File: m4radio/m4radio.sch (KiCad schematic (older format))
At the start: 72 parts, among them IC1 MCP2562, IC2 STM32F405RxTx, J1 WEST TOP, J2 EAST TOP, P1 SWD_TC, Y1 26M

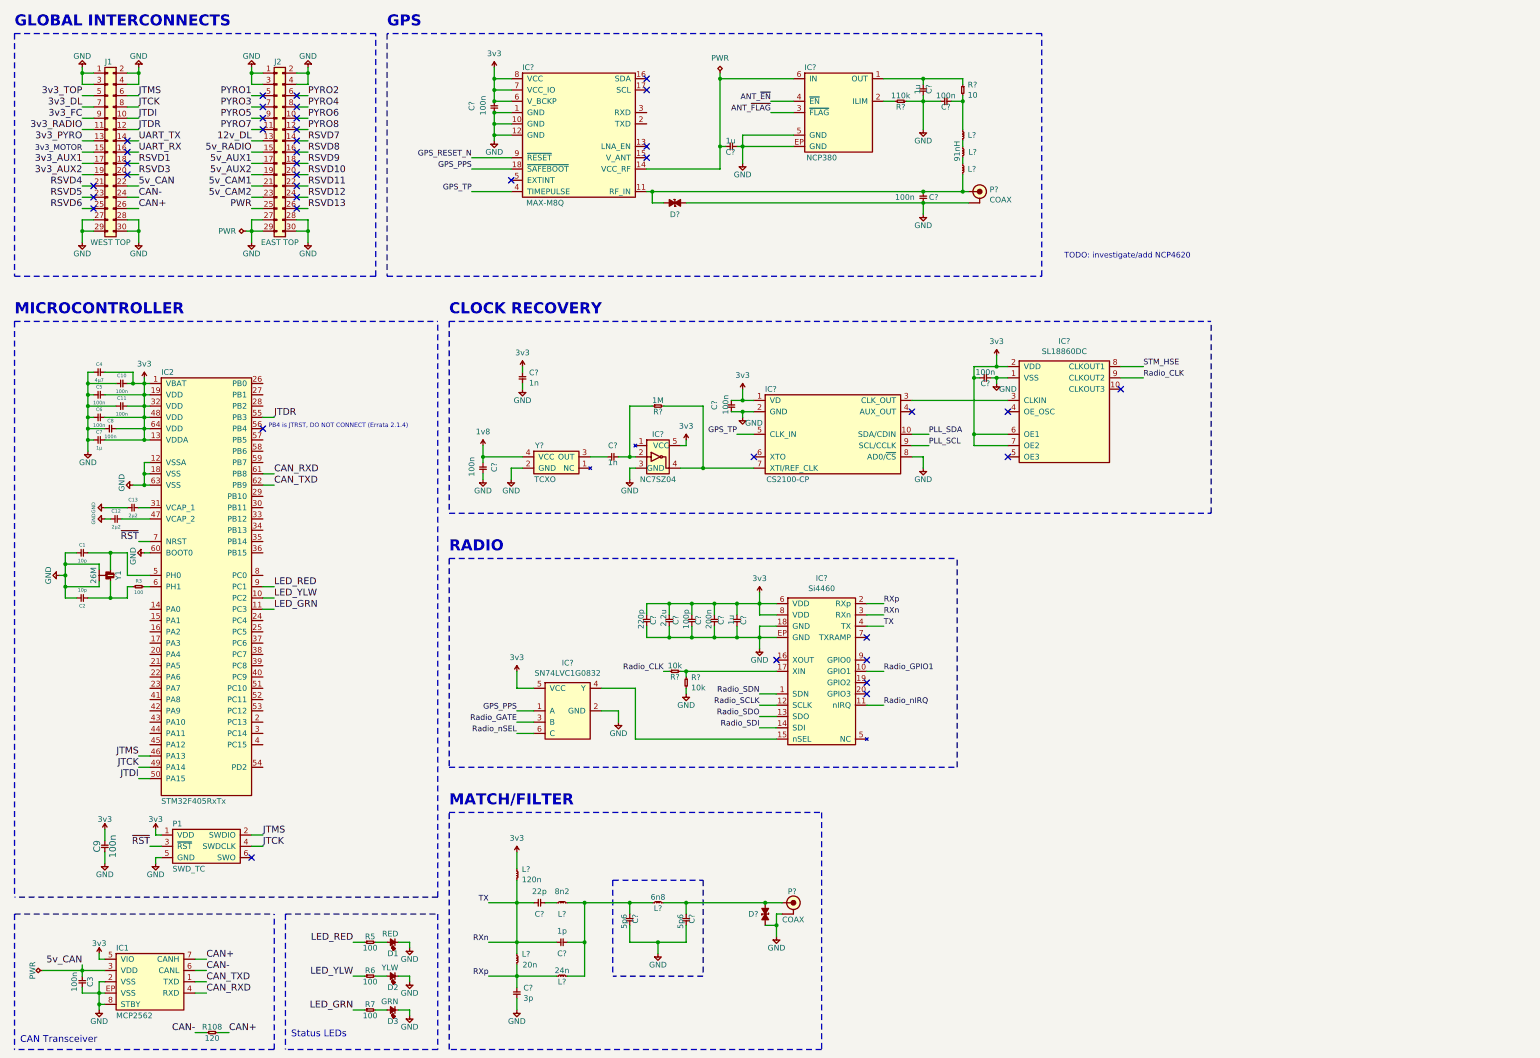
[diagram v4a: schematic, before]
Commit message: Update labels around microcontroller
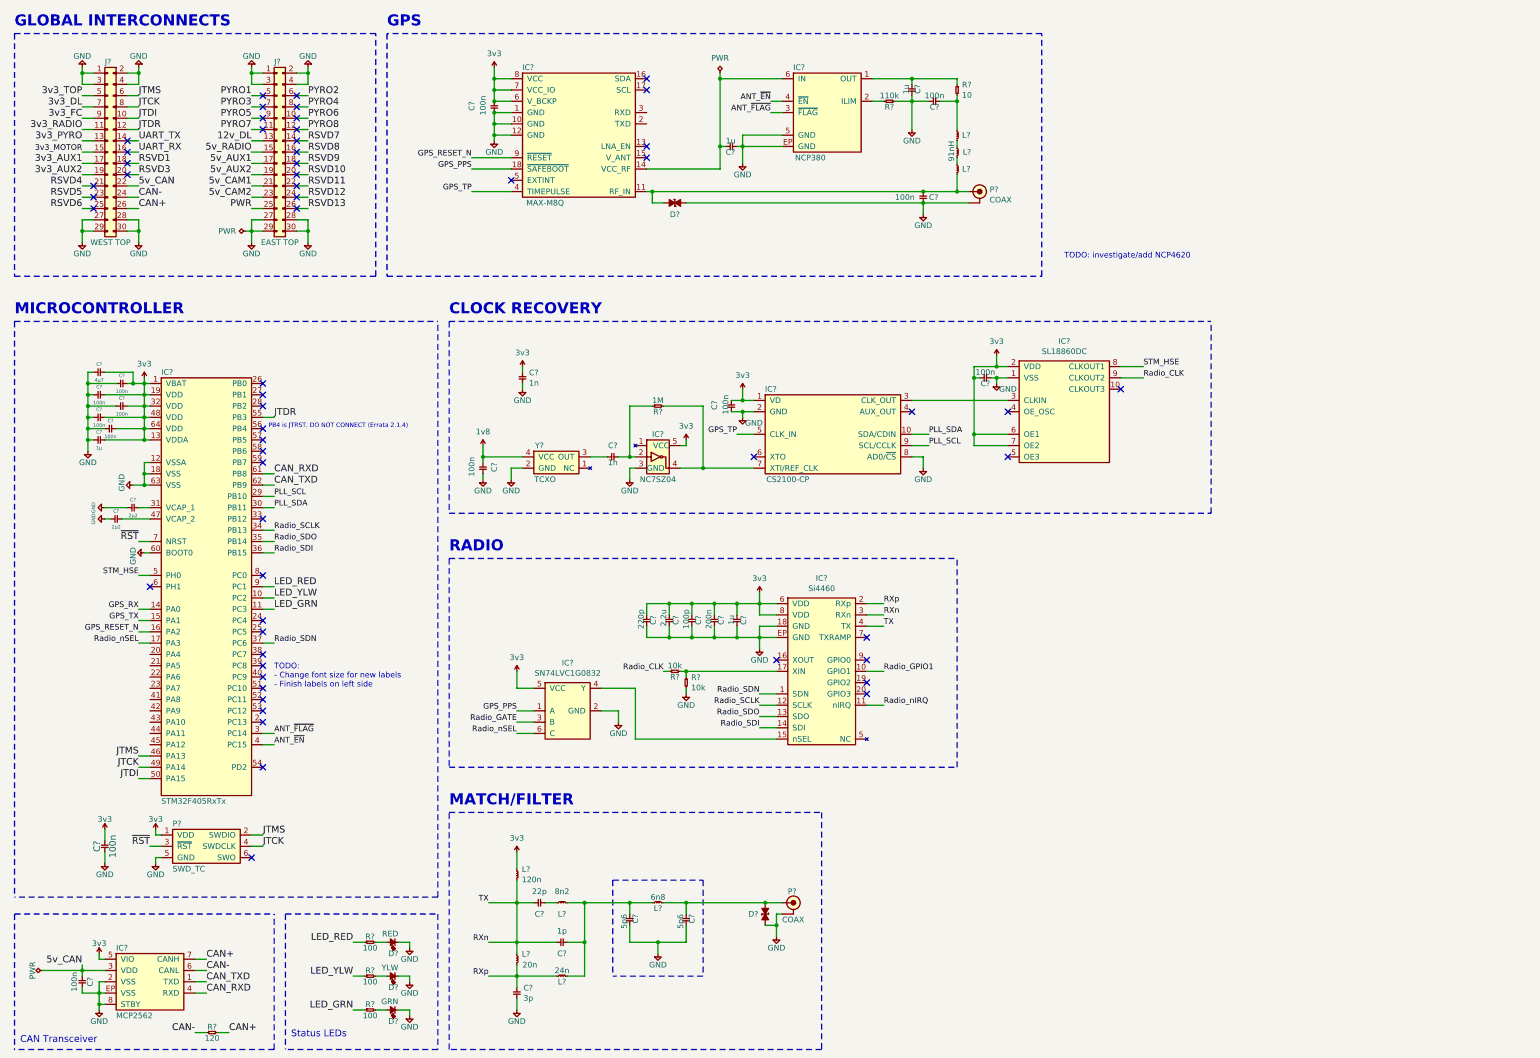
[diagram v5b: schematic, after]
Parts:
- removed C1, C2: 10p, agg:0402, symbol agg-kicad:C
- removed R3: 100, agg:0402, symbol agg-kicad:R
- removed Y1: 26M, agg:XTAL-20x16, symbol agg-kicad:SMD_XTAL
- renumbered C3 to C?, C9 to C?, C10 to C?, C7 to C?, C4 to C?, C5 to C?, C11 to C?, C6 to C?, C8 to C?, C13 to C?, C12 to C?, D1 to D?, D2 to D?, D3 to D?, IC1 to IC?, IC2 to IC?, J1 to J?, J2 to J?, P1 to P?, R108 to R?, R5 to R?, R6 to R?, R7 to R?
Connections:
- net ANT_~EN: now also IC?.4 (PC15)
- net ANT_~FLAG: now also IC?.3 (PC14)
- net GPS_RESET_N: now also IC?.16 (PA2)
- net PLL_SCL: now also IC?.29 (PB10)
- net PLL_SDA: now also IC?.30 (PB11)
- net Radio_SCLK: now also IC?.34 (PB13)
- net Radio_SDI: now also IC?.36 (PB15)
- net Radio_SDN: now also IC?.37 (PC6)
- net Radio_SDO: now also IC?.35 (PB14)
- net Radio_nSEL: now also IC?.17 (PA3)
- net STM_HSE: now also IC?.5 (PH0)
- net GPS_RX: now reaches IC?.14 (PA0)
- net GPS_TX: now reaches IC?.15 (PA1)
- no-connect marks 39 -> 58
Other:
- note added: "TODO:\n- Change font size for new labels\n- Finish labels on left side"
- moved on the sheet: C?, IC?, L?, R?

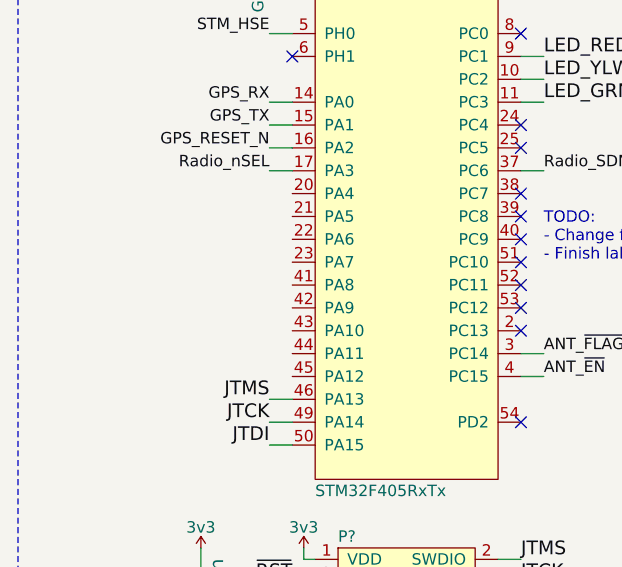
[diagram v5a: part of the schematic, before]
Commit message: Update more labels
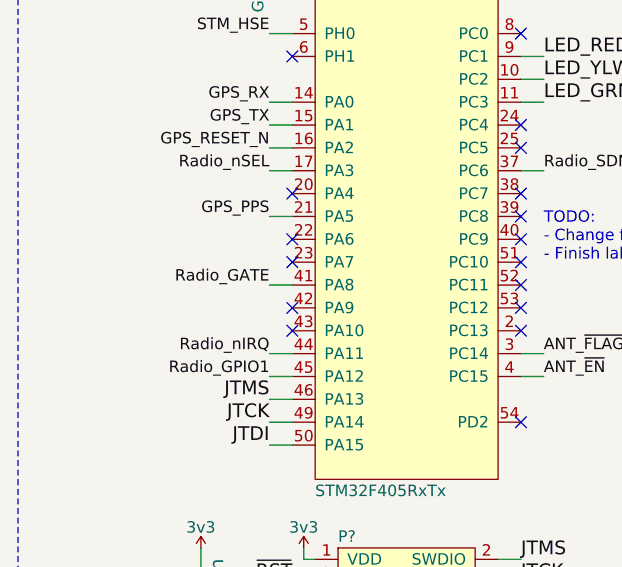
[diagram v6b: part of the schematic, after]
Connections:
- net GPS_PPS: now also IC?.21 (PA5)
- net Radio_GATE: now also IC?.41 (PA8)
- net Radio_GPIO1: now also IC?.45 (PA12)
- net Radio_nIRQ: now also IC?.44 (PA11)
- no-connect marks 58 -> 63
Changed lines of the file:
@@
 Wire Wire Line
 	9000 2200 9100 2200
+Wire Wire Line
+	1850 7100 1750 7100
+Text Label 1750 7100 2    50   ~ 0
+Radio_GPIO1
+Wire Wire Line
+	1850 7000 1750 7000
+Text Label 1750 7000 2    50   ~ 0
+Radio_nIRQ
+Wire Wire Line
+	1850 6700 1750 6700
+Text Label 1750 6700 2    50   ~ 0
+Radio_GATE
+Wire Wire Line
+	1750 6400 1850 6400
+Text Label 1750 6400 2    50   ~ 0
+GPS_PPS
+NoConn ~ 1850 6300
+NoConn ~ 1850 6500
+NoConn ~ 1850 6600
+NoConn ~ 1850 6800
+NoConn ~ 1850 6900
 $EndSCHEMATC
